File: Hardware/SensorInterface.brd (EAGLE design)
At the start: 160 x 100 mm, 49 parts, among them J3 CONN_3SCREW_254, J4 CONN_42.54_SCREW, Q1 DMG3404, Q2 2N7002, Q3 2N7002, Q4 DMG3404, Q5 DMG3404, U10 SN74AHC1G86DCK, U11 MCP6041, U12 MCP4725A1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

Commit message: +1 detector, MUX, 3V3 labels
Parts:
- added J5: CONN_42.54_SCREW, bschulz:1X04_SCREW
- added U15: SN74AUP1T157DCK, bschulz:DCK_R-PDSO-G6
- J4: value CONN_42.54_SCREW -> CONN_3SCREW_254; device bschulz:1X04_SCREW -> bschulz:1X03_SCREW
- moved J4 34.7 mm to (-52.0, -4.00)
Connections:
- new net F_IN_0: J3.2, U15.3
- new net F_IN_1: J4.2, U15.1
- new net F_IN_SW: U$3.11, U15.4
- net 3V3: now also J4.3, U15.5
- net F_IN: now also U15.6; no longer J3.2
- net GND: now also J4.1, U15.2
- net SCL_EXT: now also J5.4; no longer J4.4
- net SDA_EXT: now also J5.3; no longer J4.3
- net VIN+: now also J5.2; no longer J4.2
- net VIN-: now also J5.1; no longer J4.1
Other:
- board size 160 x 100 mm -> 72 x 20 mm

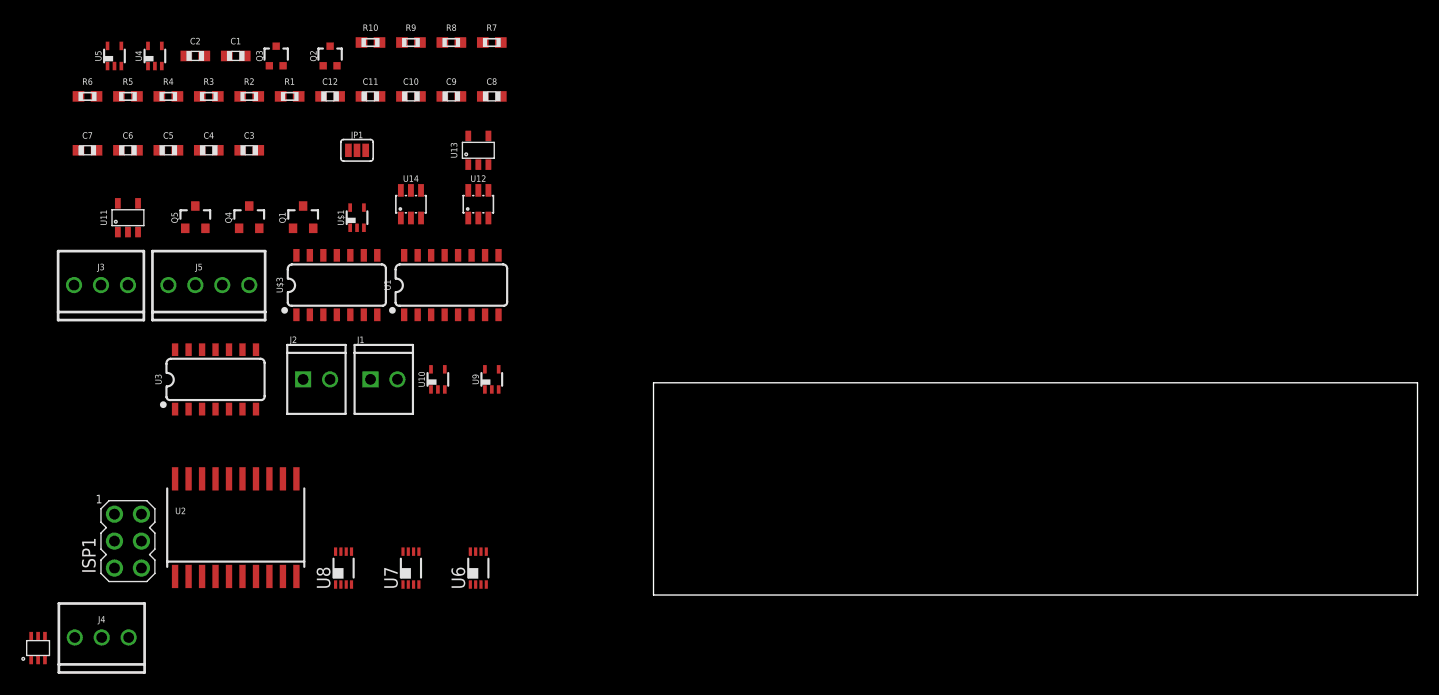
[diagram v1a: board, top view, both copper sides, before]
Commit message: LED system laid out (mostly)
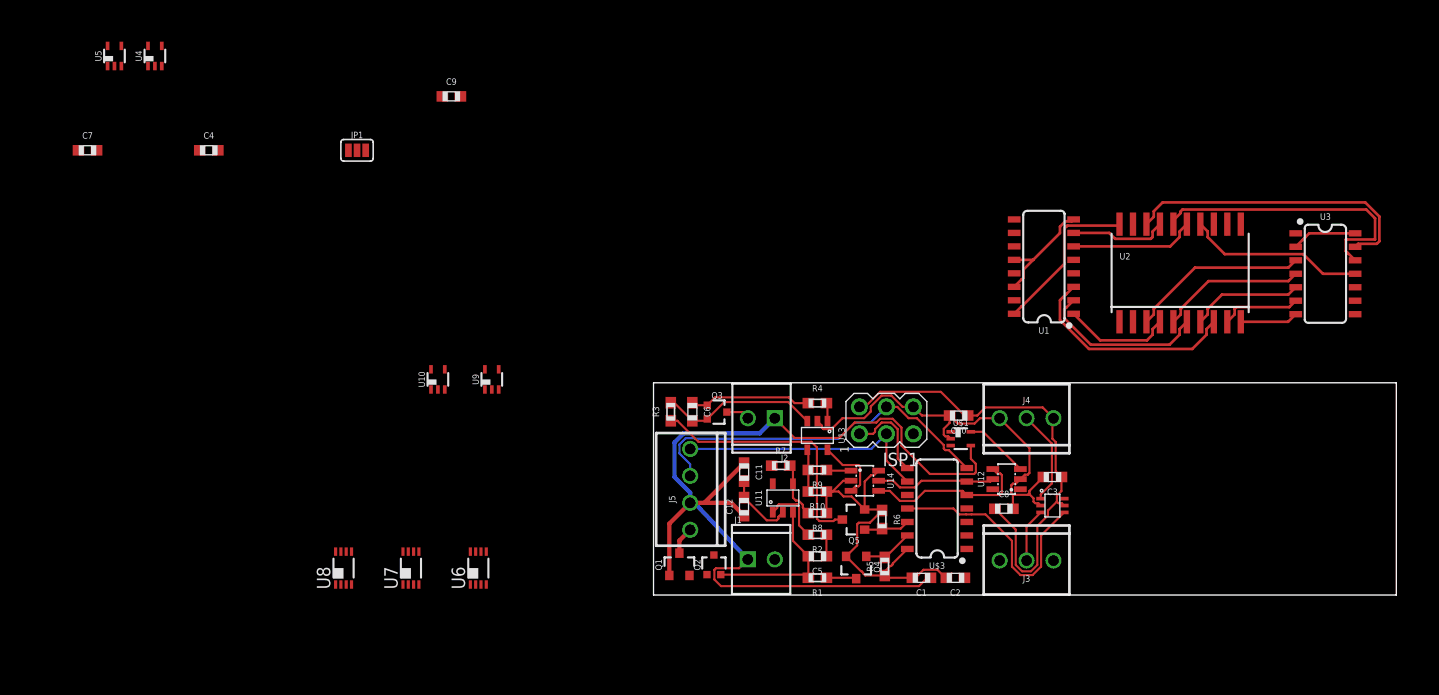
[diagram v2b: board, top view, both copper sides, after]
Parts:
- moved U3 105.8 mm to (63.3, 30.9), turned to 270 degrees
- moved U15 96.5 mm to (37.6, 8.43), turned to 270 degrees
- moved U2 92.2 mm to (49.6, 30.4)
- moved J3 91.0 mm to (35.2, 3.25), turned to 180 degrees
- moved J4 89.6 mm to (35.2, 16.7)
- moved C2 86.9 mm to (28.4, 1.63), turned to 180 degrees
- moved R6 84.8 mm to (21.5, 7.11), turned to 270 degrees
- moved R5 84.0 mm to (21.8, 2.69), turned to 90 degrees
- moved C3 81.7 mm to (37.6, 11.1), turned to 180 degrees
- moved C1 81.2 mm to (25.2, 1.63), turned to 180 degrees
- moved ISP1 72.4 mm to (21.9, 16.5), turned to 90 degrees
- moved C5 72.1 mm to (15.4, 3.66), turned to 180 degrees
- moved Q5 68.3 mm to (18.9, 7.11), turned to 90 degrees
- moved R4 67.6 mm to (15.4, 18.1)
- moved R2 67.6 mm to (15.4, 5.69), turned to 180 degrees
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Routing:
- net GND: track 0.00 -> 98.4 mm
- net VIN+: track 0.00 -> 94.8 mm
- net 3V3: track 0.00 -> 79.4 mm
- net SDA_EXT: track 0.00 -> 34.6 mm
- net N$16: track 0.00 -> 28.5 mm
- net N$15: track 0.00 -> 27.3 mm
- net SCL_EXT: track 0.00 -> 24.4 mm
- net N$26: track 0.00 -> 24.1 mm
- net F_IN_SW: track 0.00 -> 23.0 mm
- net N$4: track 0.00 -> 20.7 mm
- net N$14: track 0.00 -> 16.8 mm
- net N$9: track 0.00 -> 16.8 mm
- net N$3: track 0.00 -> 15.9 mm
- net SDA: track 0.00 -> 15.4 mm
- net N$22: track 0.00 -> 15.1 mm
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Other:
- board size 72 x 20 mm -> 70 x 20 mm

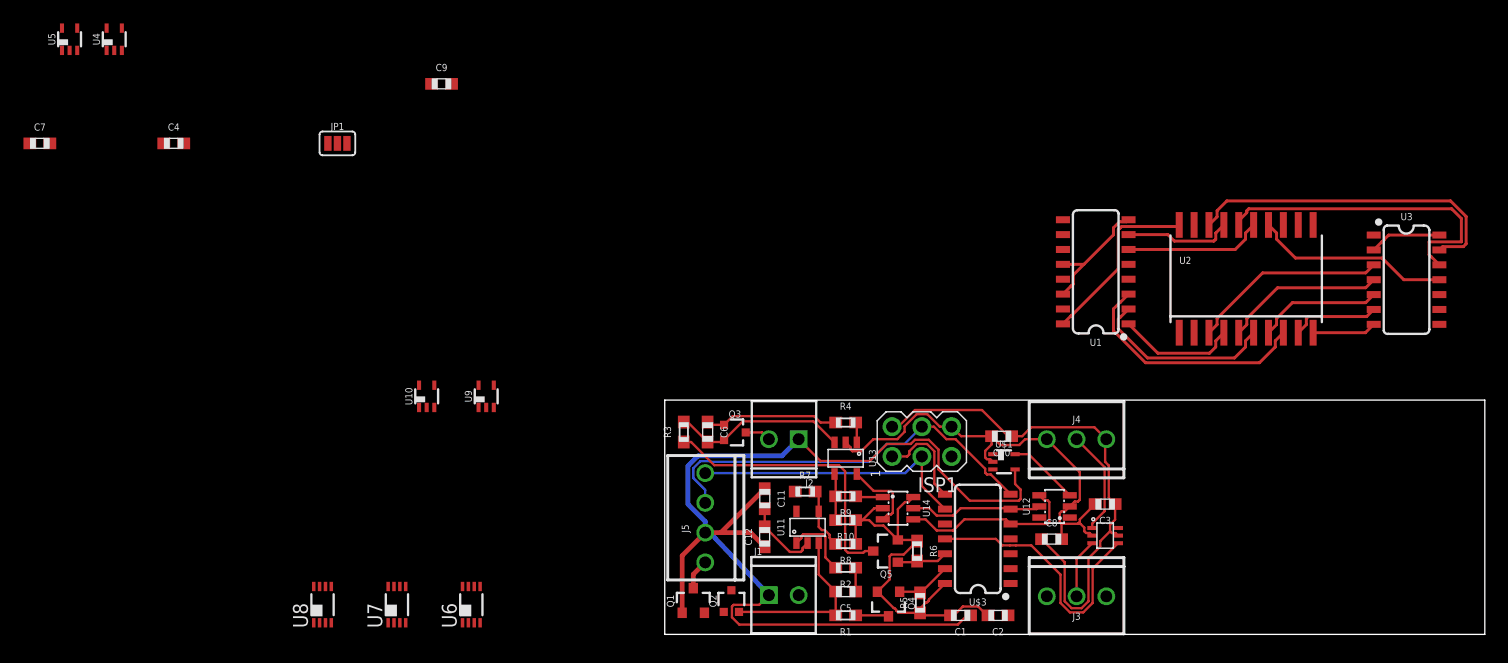
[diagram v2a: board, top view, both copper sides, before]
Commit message: Initial routing complete with DRC
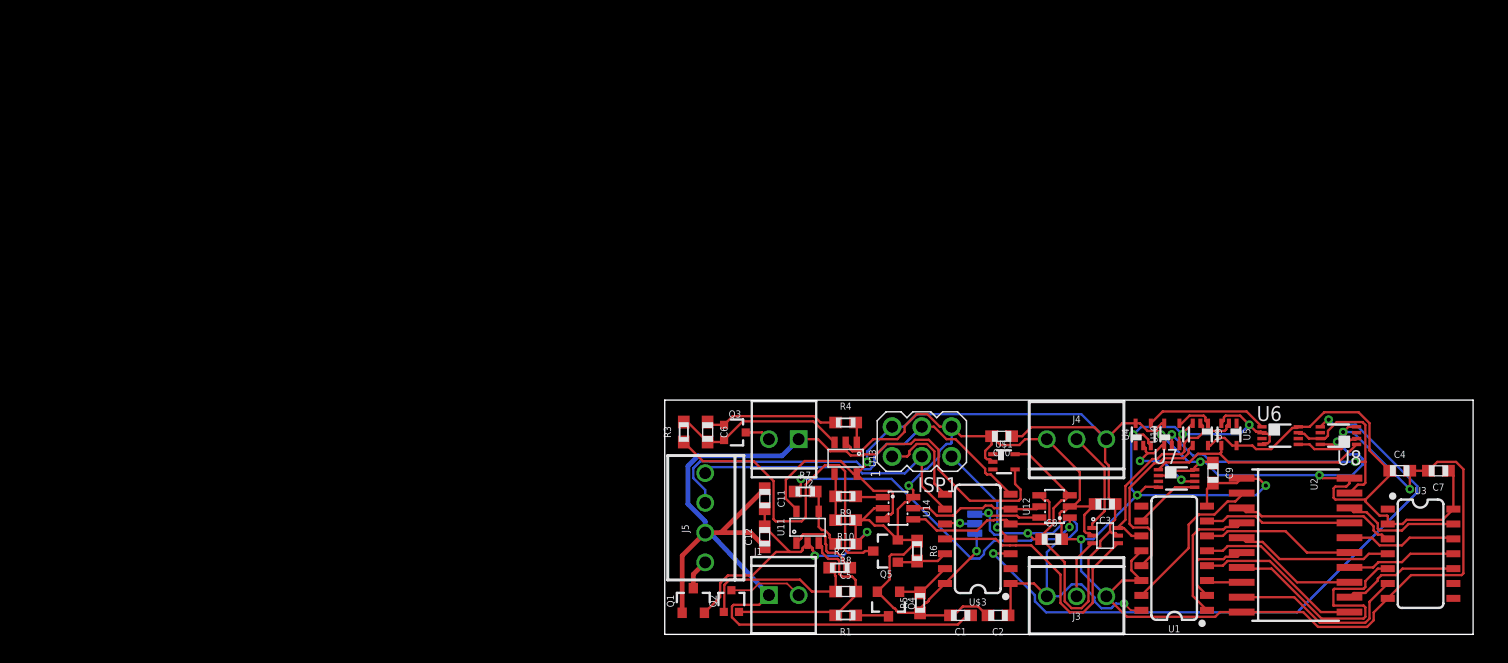
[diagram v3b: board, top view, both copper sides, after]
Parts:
- moved C7 122.6 mm to (66.0, 14.0), turned to 180 degrees
- moved C4 108.3 mm to (62.7, 14.0)
- moved U5 104.5 mm to (48.2, 17.1), turned to 180 degrees
- moved U4 94.1 mm to (40.8, 17.1)
- moved U8 87.9 mm to (57.5, 17.0), turned to 90 degrees
- moved C9 73.7 mm to (46.8, 13.8), turned to 270 degrees
- moved U6 70.5 mm to (52.5, 17.0), turned to 270 degrees
- moved U7 67.4 mm to (43.7, 13.3), turned to 270 degrees
- moved U10 63.7 mm to (43.3, 17.1)
- moved JP1 63.4 mm to (26.5, 9.45), flipped to the bottom, turned to 270 degrees
- moved U9 61.0 mm to (45.7, 17.1), turned to 180 degrees
- moved U1 25.3 mm to (43.5, 6.50)
- moved U3 23.4 mm to (64.5, 7.52)
- moved U2 23.1 mm to (53.8, 7.62), turned to 270 degrees
- moved R2 0.51 mm to (14.9, 5.69), turned to 0 degrees
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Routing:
- net GND: track 98.4 -> 241.0 mm, vias 0 -> 12
- net 3V3: track 79.4 -> 208.4 mm, vias 0 -> 8
- net !INT: track 0.00 -> 55.7 mm, vias 0 -> 2
- net !P=Q: track 0.00 -> 32.0 mm, vias 0 -> 2
- net N$28: track 0.00 -> 29.1 mm, vias 0 -> 2
- net !F_IN: track 0.00 -> 19.2 mm
- net F_IN: track 0.00 -> 18.6 mm
- net N$16: track 28.5 -> 10.2 mm
- net N$15: track 27.3 -> 9.45 mm
- net N$4: track 20.7 -> 3.03 mm
- net RCLK: track 0.00 -> 15.6 mm
- net N$5: track 0.00 -> 14.1 mm
- net N$6: track 0.00 -> 13.6 mm
- net N$1: track 0.00 -> 13.5 mm
- net N$23: track 2.03 -> 14.7 mm
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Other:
- board size 70 x 20 mm -> 69 x 20 mm

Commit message: Silkscreen for initial prototype
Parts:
- added LOGO1: OSHW-LOGOM, SparkFun-Aesthetics:OSHW-LOGO-M
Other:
- board text added: "Project Calypso v0.0.0 2018.12.23 Bobby Schulz (schematic) Andy Wickert (layout) UMN senior design team (basis design) Design: Northern Widget LLC in collaboration with The University of Minnesota"
- board text added: "Turbidity sensor: Light and detector control board"
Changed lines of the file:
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@@
 <layer number="23" name="tOrigins" color="15" fill="1" visible="yes" active="yes"/>
 <layer number="24" name="bOrigins" color="15" fill="1" visible="yes" active="yes"/>
-<layer number="25" name="tNames" color="7" fill="1" visible="yes" active="yes"/>
-<layer number="26" name="bNames" color="7" fill="1" visible="yes" active="yes"/>
-<layer number="27" name="tValues" color="7" fill="1" visible="yes" active="yes"/>
-<layer number="28" name="bValues" color="7" fill="1" visible="yes" active="yes"/>
+<layer number="25" name="tNames" color="7" fill="1" visible="no" active="yes"/>
+<layer number="26" name="bNames" color="7" fill="1" visible="no" active="yes"/>
+<layer number="27" name="tValues" color="7" fill="1" visible="no" active="yes"/>
+<layer number="28" name="bValues" color="7" fill="1" visible="no" active="yes"/>
 <layer number="29" name="tStop" color="7" fill="3" visible="no" active="yes"/>
 <layer number="30" name="bStop" color="7" fill="6" visible="no" active="yes"/>
@@
 <layer number="37" name="tTest" color="7" fill="1" visible="no" active="yes"/>
 <layer number="38" name="bTest" color="7" fill="1" visible="no" active="yes"/>
-<layer number="39" name="tKeepout" color="4" fill="11" visible="yes" active="yes"/>
-<layer number="40" name="bKeepout" color="1" fill="11" visible="yes" active="yes"/>
-<layer number="41" name="tRestrict" color="4" fill="10" visible="yes" active="yes"/>
-<layer number="42" name="bRestrict" color="1" fill="10" visible="yes" active="yes"/>
-<layer number="43" name="vRestrict" color="2" fill="10" visible="yes" active="yes"/>
+<layer number="39" name="tKeepout" color="4" fill="11" visible="no" active="yes"/>
+<layer number="40" name="bKeepout" color="1" fill="11" visible="no" active="yes"/>
+<layer number="41" name="tRestrict" color="4" fill="10" visible="no" active="yes"/>
+<layer number="42" name="bRestrict" color="1" fill="10" visible="no" active="yes"/>
+<layer number="43" name="vRestrict" color="2" fill="10" visible="no" active="yes"/>
 <layer number="44" name="Drills" color="7" fill="1" visible="no" active="yes"/>
 <layer number="45" name="Holes" color="7" fill="1" visible="no" active="yes"/>
 <layer number="46" name="Milling" color="3" fill="1" visible="no" active="yes"/>
 <layer number="47" name="Measures" color="7" fill="1" visible="no" active="yes"/>
-<layer number="48" name="Document" color="7" fill="1" visible="yes" active="yes"/>
-<layer number="49" name="Reference" color="7" fill="1" visible="yes" active="yes"/>
+<layer number="48" name="Document" color="7" fill="1" visible="no" active="yes"/>
+<layer number="49" name="Reference" color="7" fill="1" visible="no" active="yes"/>
 <layer number="50" name="dxf" color="7" fill="1" visible="no" active="no"/>
 <layer number="51" name="tDocu" color="7" fill="1" visible="yes" active="yes"/>
@@
 <wire x1="69" y1="20" x2="0" y2="20" width="0" layer="20"/>
 <wire x1="0" y1="20" x2="0" y2="0" width="0" layer="20"/>
+<text x="67.564" y="2.032" size="1.27" layer="52" rot="MR0">Project Calypso v0.0.0
+2018.12.23
+Bobby Schulz (schematic)
+Andy Wickert (layout)
+UMN senior design team (basis design)
+Design: Northern Widget LLC
+in collaboration with
+The University of Minnesota</text>
+<text x="25.4" y="1.016" size="1.27" layer="52" rot="MR0">Turbidity sensor:
+Light and detector control board</text>
 </plain>
 <attributes>
@@
 <attribute name="MPN" value="SN74AUP1T157DCKR" x="37.592" y="8.4328" size="1.778" layer="27" rot="R270" display="off"/>
 </element>
+<element name="LOGO1" library="SparkFun-Aesthetics" package="OSHW-LOGO-M" value="OSHW-LOGOM" x="64.516" y="16.764"/>
 </elements>
 <signals>
@@
 </drawing>
 <compatibility>
+<note version="6.3" minversion="6.2.2" severity="warning">
+Since Version 6.2.2 text objects can contain more than one line,
+which will not be processed correctly with this version.
+</note>
 <note version="8.2" severity="warning">
 Since Version 8.2, EAGLE supports online libraries. The ids
